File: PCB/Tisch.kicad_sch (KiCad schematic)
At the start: 7 parts, among them U1 ADAU1451, U2 PCM5122PW, U3 Microchip_BM83, U4 ESP32-S3-WROOM-1, U5 TS3USB221DRCR, U6 XU208-128-TQ64-C10, U7 DIR9001PWR

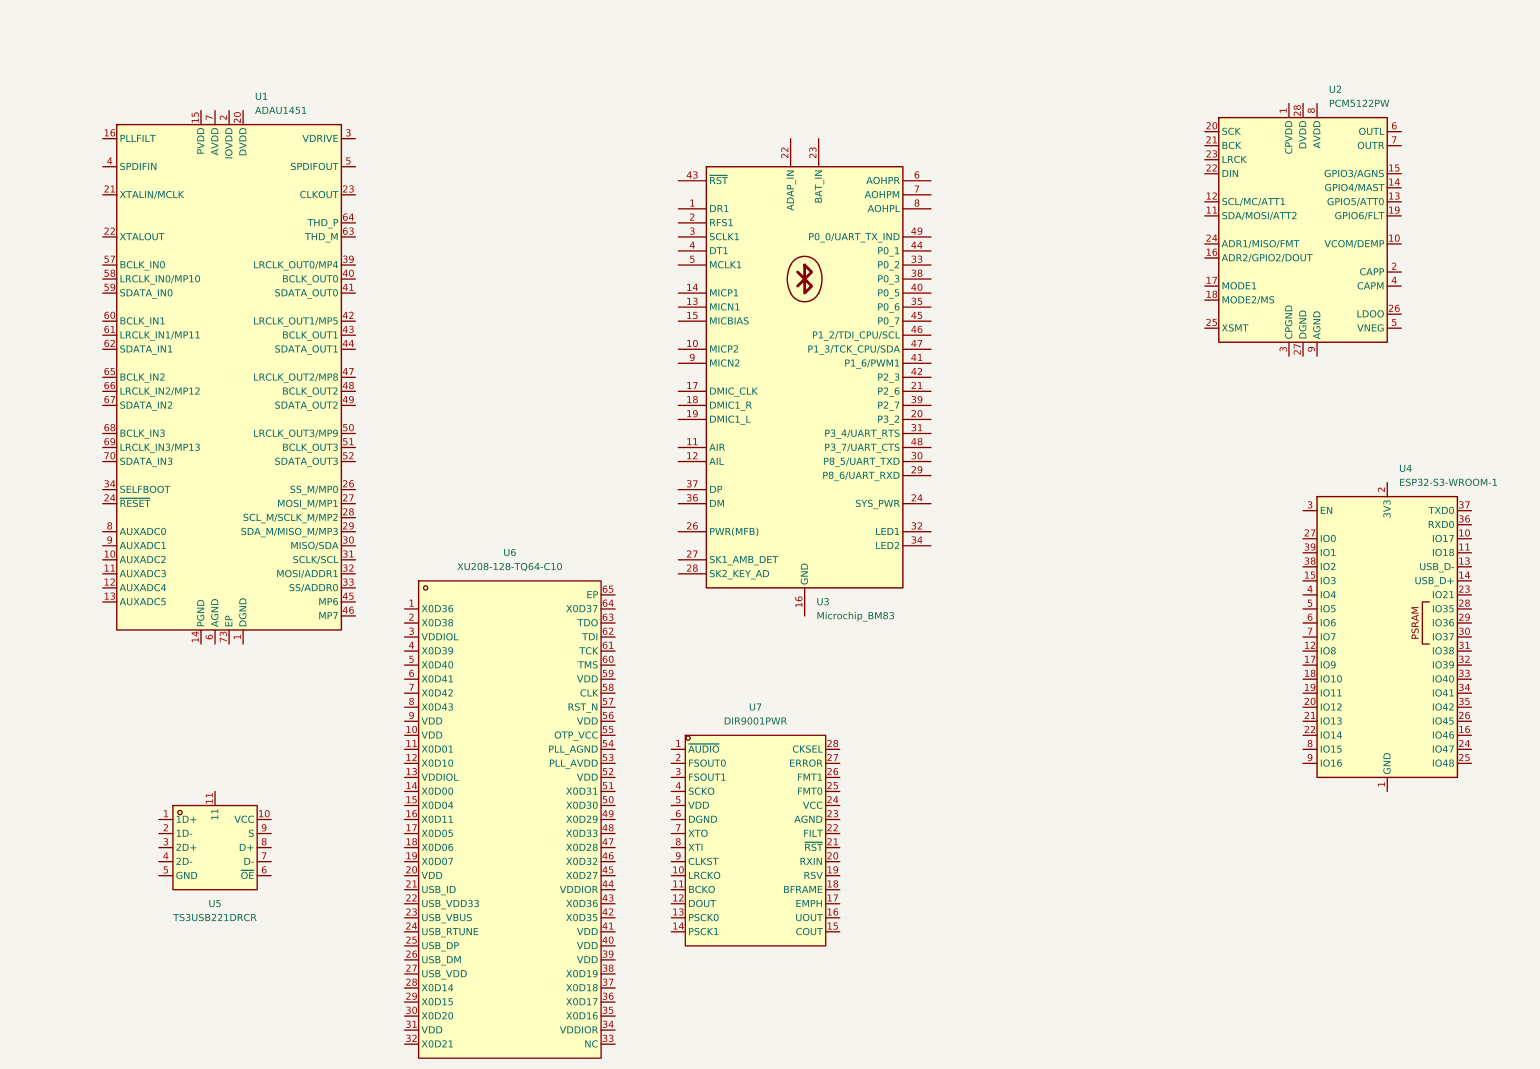
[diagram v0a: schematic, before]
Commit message: added Raspi, ESP32 etc
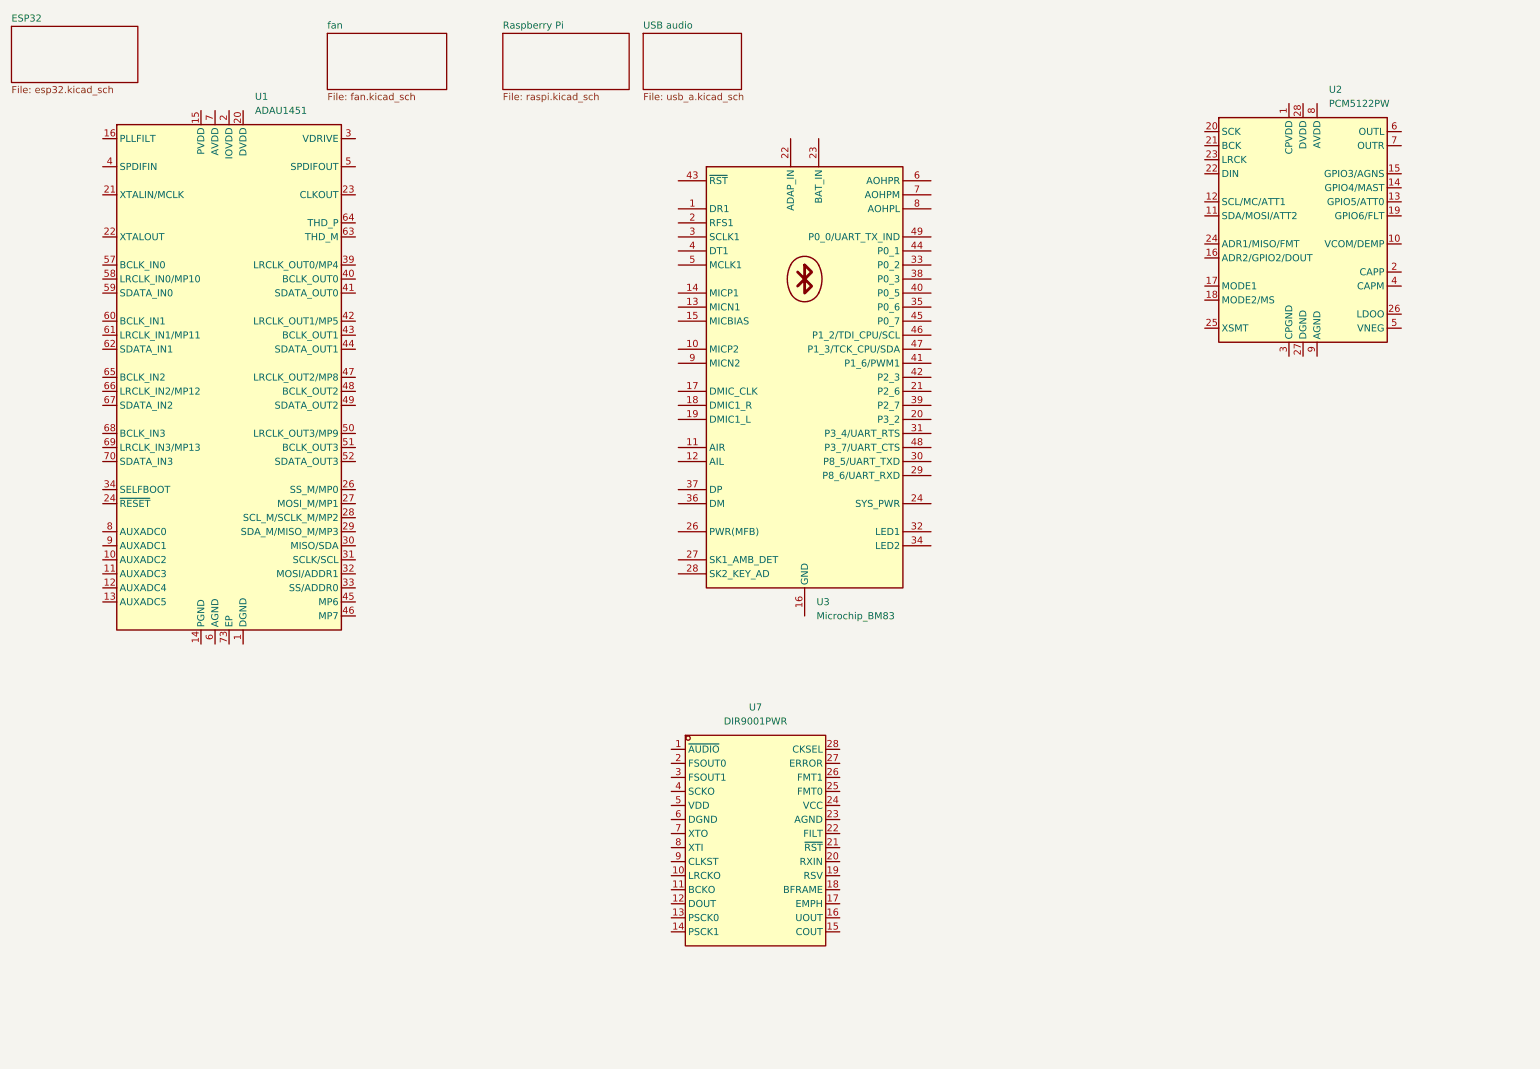
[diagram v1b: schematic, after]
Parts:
- removed U4: ESP32-S3-WROOM-1, RF_Module:ESP32-S3-WROOM-1U, symbol RF_Module:ESP32-S3-WROOM-1
- removed U5: TS3USB221DRCR, easyeda2kicad:VSON-10_L3.0-W3.0-P0.50-TL-EP_TPS62410DRCR, symbol easyeda2kicad:TS3USB221DRCR
- removed U6: XU208-128-TQ64-C10, easyeda2kicad:TQFP-64_L10.0-W10.0-P0.50-LS12.0-BL-EP5.3, symbol easyeda2kicad:XU208-128-TQ64-C10
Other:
- added sheet ESP32 (esp32.kicad_sch)
- added sheet Raspberry Pi (raspi.kicad_sch)
- added sheet USB audio (usb_a.kicad_sch)
- added sheet fan (fan.kicad_sch)

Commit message: Initial commit of project source code
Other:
- added sheet QCC5125 (QCC5125.kicad_sch)
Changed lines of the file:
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@@
+	)
+	(sheet
+		(at 148.59 13.97)
+		(size 15.24 10.16)
+		(exclude_from_sim no)
+		(in_bom yes)
+		(on_board yes)
+		(dnp no)
+		(fields_autoplaced yes)
+		(stroke
+			(width 0.1524)
+			(type solid)
+		)
+		(fill
+			(color 0 0 0 0.0000)
+		)
+		(property "Sheetname" "QCC5125"
+			(at 148.59 13.2584 0)
+			(effects
+				(font
+					(size 1.27 1.27)
+				)
+				(justify left bottom)
+			)
+		)
+		(property "Sheetfile" "QCC5125.kicad_sch"
+			(at 148.59 24.7146 0)
+			(effects
+				(font
+					(size 1.27 1.27)
+				)
+				(justify left top)
+			)
+		)
+		(instances
+			(project "Tisch"
+				(path "/08b9944e-0e9a-4685-98da-9a654683b13c"
+					(page "6")
+				)
+			)
+		)
 	)
 	(sheet

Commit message: feat: Improve .gitignore and remove tracked binaries/backups
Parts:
- removed U7: DIR9001PWR, easyeda2kicad:TSSOP-28_L9.7-W4.4-P0.65-LS6.4-BL, symbol easyeda2kicad:DIR9001PWR
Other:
- added sheet SPdif (spdif.kicad_sch)
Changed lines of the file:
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@@
-	)
-	(symbol
-		(lib_id "easyeda2kicad:DIR9001PWR")
-		(at 147.32 160.02 0)
-		(unit 1)
-		(exclude_from_sim no)
-		(in_bom yes)
-		(on_board yes)
-		(dnp no)
-		(fields_autoplaced yes)
-		(property "Reference" "U7"
-			(at 147.32 135.89 0)
-			(effects
-				(font
-					(size 1.27 1.27)
-				)
-			)
-		)
-		(property "Value" "DIR9001PWR"
-			(at 147.32 138.43 0)
-			(effects
-				(font
-					(size 1.27 1.27)
-				)
-			)
-		)
-		(property "Footprint" "easyeda2kicad:TSSOP-28_L9.7-W4.4-P0.65-LS6.4-BL"
-			(at 147.32 184.15 0)
-			(effects
-				(font
-					(size 1.27 1.27)
-				)
-				(hide yes)
-			)
-		)
-		(property "Datasheet" "https://lcsc.com/product-detail/Others_Texas-Instruments_DIR9001PWR_Texas-Instruments-TI-DIR9001PWR_C96215.html"
-			(at 147.32 186.69 0)
-			(effects
-				(font
-					(size 1.27 1.27)
-				)
-				(hide yes)
-			)
-		)
-		(property "Description" ""
-			(at 147.32 160.02 0)
-			(effects
-				(font
-					(size 1.27 1.27)
-				)
-				(hide yes)
-			)
-		)
-		(property "LCSC Part" "C96215"
-			(at 147.32 189.23 0)
-			(effects
-				(font
-					(size 1.27 1.27)
-				)
-				(hide yes)
-			)
-		)
-		(pin "16"
-		)
-		(pin "12"
-		)
-		(pin "18"
-		)
-		(pin "23"
-		)
-		(pin "15"
-		)
-		(pin "11"
-		)
-		(pin "19"
-		)
-		(pin "17"
-		)
-		(pin "28"
-		)
-		(pin "9"
-		)
-		(pin "26"
-		)
-		(pin "27"
-		)
-		(pin "13"
-		)
-		(pin "6"
-		)
-		(pin "1"
-		)
-		(pin "10"
-		)
-		(pin "8"
-		)
-		(pin "7"
-		)
-		(pin "5"
-		)
-		(pin "25"
-		)
-		(pin "2"
-		)
-		(pin "21"
-		)
-		(pin "20"
-		)
-		(pin "4"
-		)
-		(pin "14"
-		)
-		(pin "24"
-		)
-		(pin "3"
-		)
-		(pin "22"
-		)
-		(instances
-			(project ""
-				(path "/08b9944e-0e9a-4685-98da-9a654683b13c"
-					(reference "U7")
-					(unit 1)
-				)
-			)
-		)
 	)
 	(symbol
@@
 				)
 			)
+		)
+	)
+	(sheet
+		(at 175.26 13.97)
+		(size 16.51 10.16)
+		(exclude_from_sim no)
+		(in_bom yes)
+		(on_board yes)
+		(dnp no)
+		(fields_autoplaced yes)
+		(stroke
+			(width 0.1524)
+			(type solid)
+		)
+		(fill
+			(color 0 0 0 0.0000)
+		)
+		(property "Sheetname" "SPdif"
+			(at 175.26 13.2584 0)
+			(effects
+				(font
+					(size 1.27 1.27)
+				)
+				(justify left bottom)
+			)
+		)
+		(property "Sheetfile" "spdif.kicad_sch"
+			(at 175.26 24.7146 0)
+			(effects
+				(font
+					(size 1.27 1.27)
+				)
+				(justify left top)
+			)
+		)
+		(instances
+			(project "Tisch"
+				(path "/08b9944e-0e9a-4685-98da-9a654683b13c"
+					(page "7")
+				)
+			)

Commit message: fix: Correct .gitignore for #auto_saved_files and update project
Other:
- added sheet ADC (adc.kicad_sch)
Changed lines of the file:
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@@
+	)
+	(sheet
+		(at 198.12 13.97)
+		(size 19.05 10.16)
+		(exclude_from_sim no)
+		(in_bom yes)
+		(on_board yes)
+		(dnp no)
+		(fields_autoplaced yes)
+		(stroke
+			(width 0.1524)
+			(type solid)
+		)
+		(fill
+			(color 0 0 0 0.0000)
+		)
+		(property "Sheetname" "ADC"
+			(at 198.12 13.2584 0)
+			(effects
+				(font
+					(size 1.27 1.27)
+				)
+				(justify left bottom)
+			)
+		)
+		(property "Sheetfile" "adc.kicad_sch"
+			(at 198.12 24.7146 0)
+			(effects
+				(font
+					(size 1.27 1.27)
+				)
+				(justify left top)
+			)
+		)
+		(instances
+			(project "Tisch"
+				(path "/08b9944e-0e9a-4685-98da-9a654683b13c"
+					(page "8")
+				)
+			)
+		)
 	)
 	(sheet

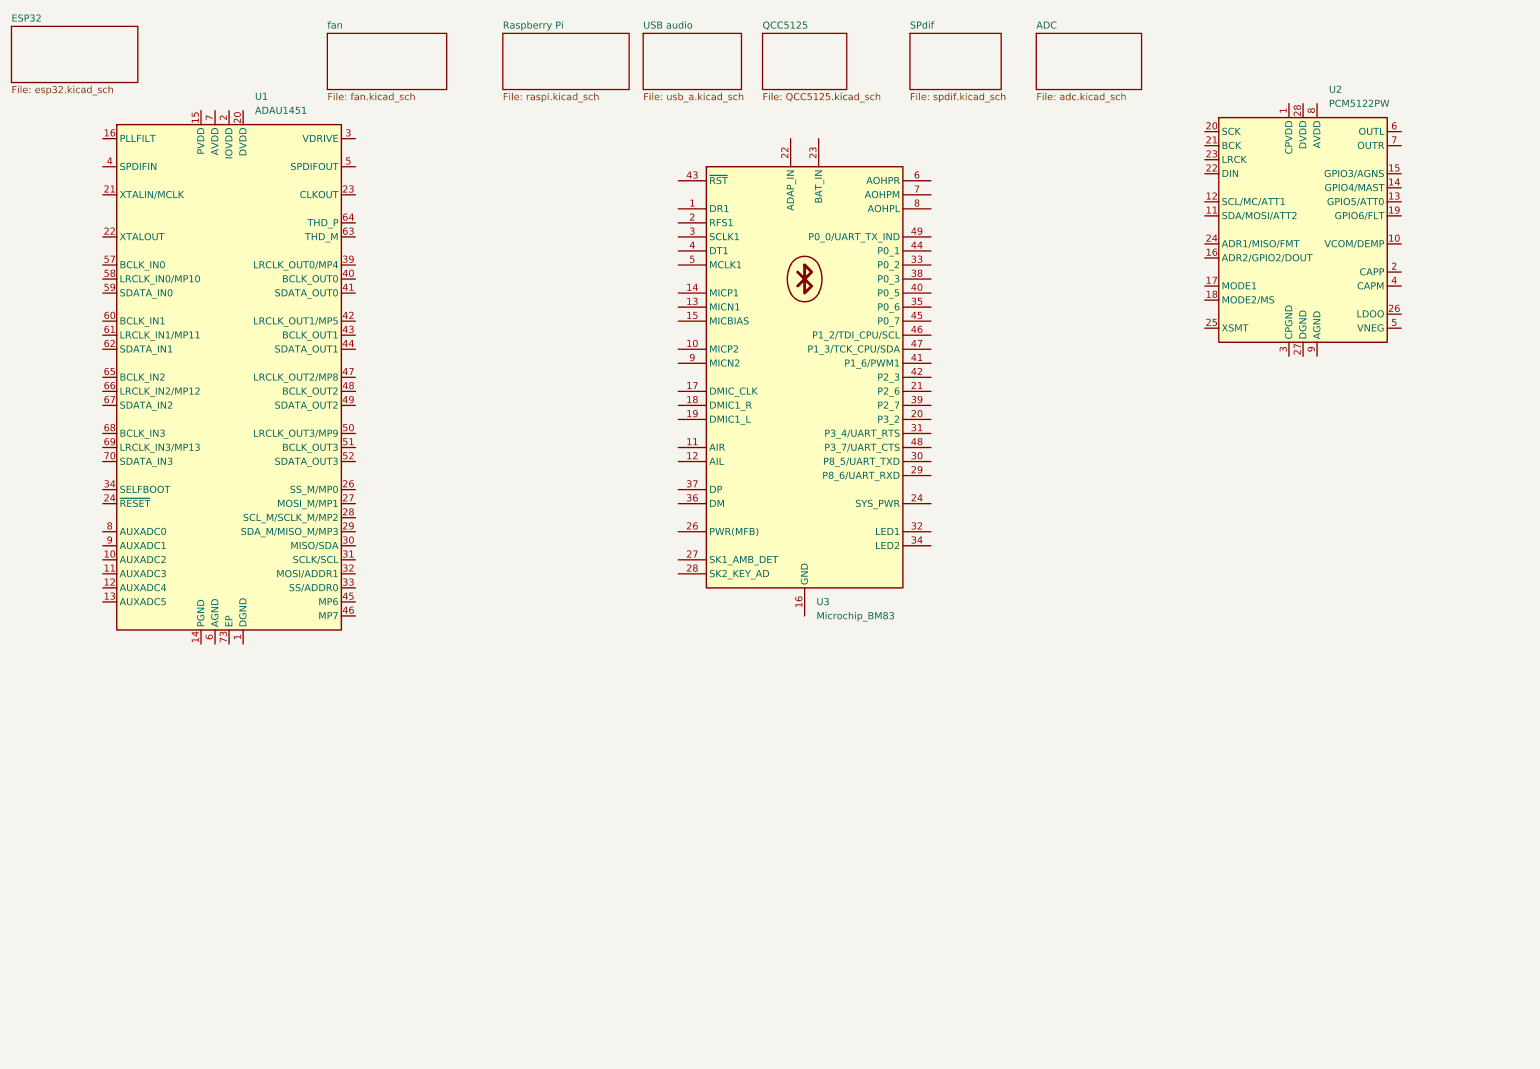
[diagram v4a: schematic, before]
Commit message: updated schematics
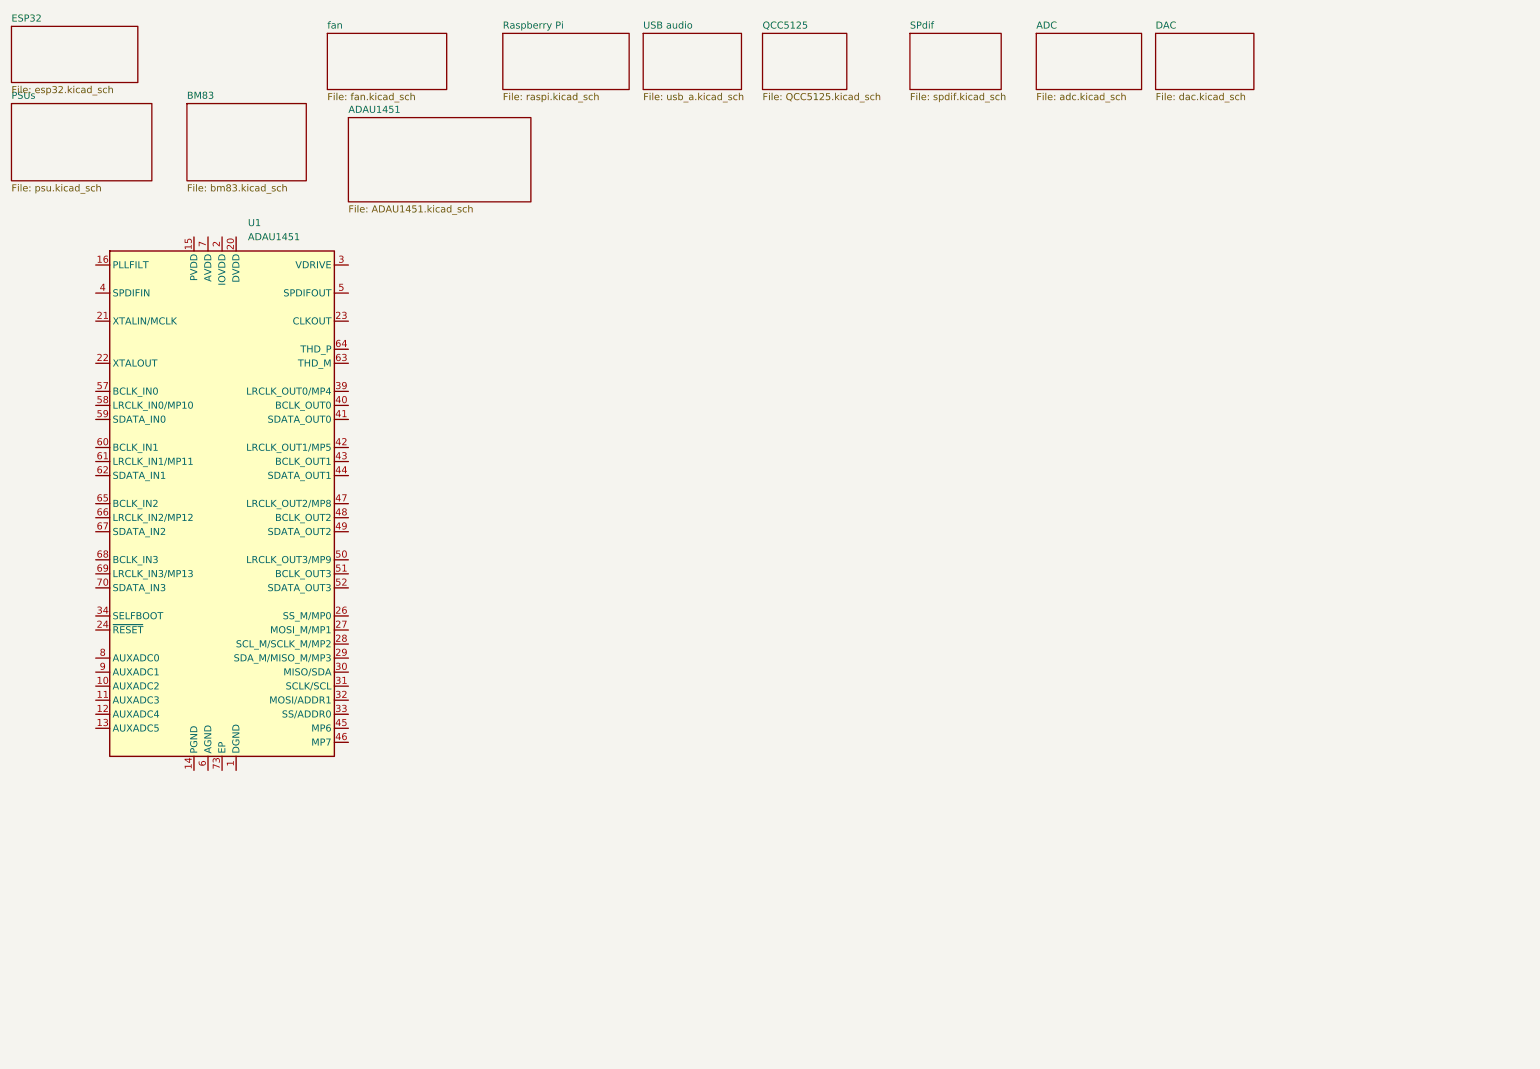
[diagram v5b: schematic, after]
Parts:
- removed U2: PCM5122PW, Package_SO:TSSOP-28_4.4x9.7mm_P0.65mm, symbol Audio:PCM5122PW
- removed U3: Microchip_BM83, RF_Module:Microchip_BM83, symbol RF_Bluetooth:Microchip_BM83
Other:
- added sheet ADAU1451 (ADAU1451.kicad_sch)
- added sheet BM83 (bm83.kicad_sch)
- added sheet DAC (dac.kicad_sch)
- added sheet PSUs (psu.kicad_sch)
- moved on the sheet: U1

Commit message: updated schematics and  added MSP4030 Docs
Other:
- added sheet HID (hid.kicad_sch)
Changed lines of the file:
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@@
+	)
+	(sheet
+		(at 209.55 60.96)
+		(size 27.94 19.05)
+		(exclude_from_sim no)
+		(in_bom yes)
+		(on_board yes)
+		(dnp no)
+		(fields_autoplaced yes)
+		(stroke
+			(width 0.1524)
+			(type solid)
+		)
+		(fill
+			(color 0 0 0 0.0000)
+		)
+		(property "Sheetname" "HID"
+			(at 209.55 60.2484 0)
+			(effects
+				(font
+					(size 1.27 1.27)
+				)
+				(justify left bottom)
+			)
+		)
+		(property "Sheetfile" "hid.kicad_sch"
+			(at 209.55 80.5946 0)
+			(effects
+				(font
+					(size 1.27 1.27)
+				)
+				(justify left top)
+			)
+		)
+		(instances
+			(project "Tisch"
+				(path "/08b9944e-0e9a-4685-98da-9a654683b13c"
+					(page "13")
+				)
+			)
+		)
 	)
 	(sheet
